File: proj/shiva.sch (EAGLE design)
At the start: 22 parts, among them J1 DM3D-SFDM, J2 ADAFRUIT_OLED_13, SW1 TACTSWB3SL-10XXP, SW2 TACTSWB3SL-10XXP, SW3 TACTSWB3SL-10XXP, SW4 TACTSWB3SL-10XXP, SW5 TACTSWB3SL-10XXP, SW6 TACTSWB3SL-10XXP, SW7 TACTSWB3SL-10XXP, U1 MCP23008QFN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

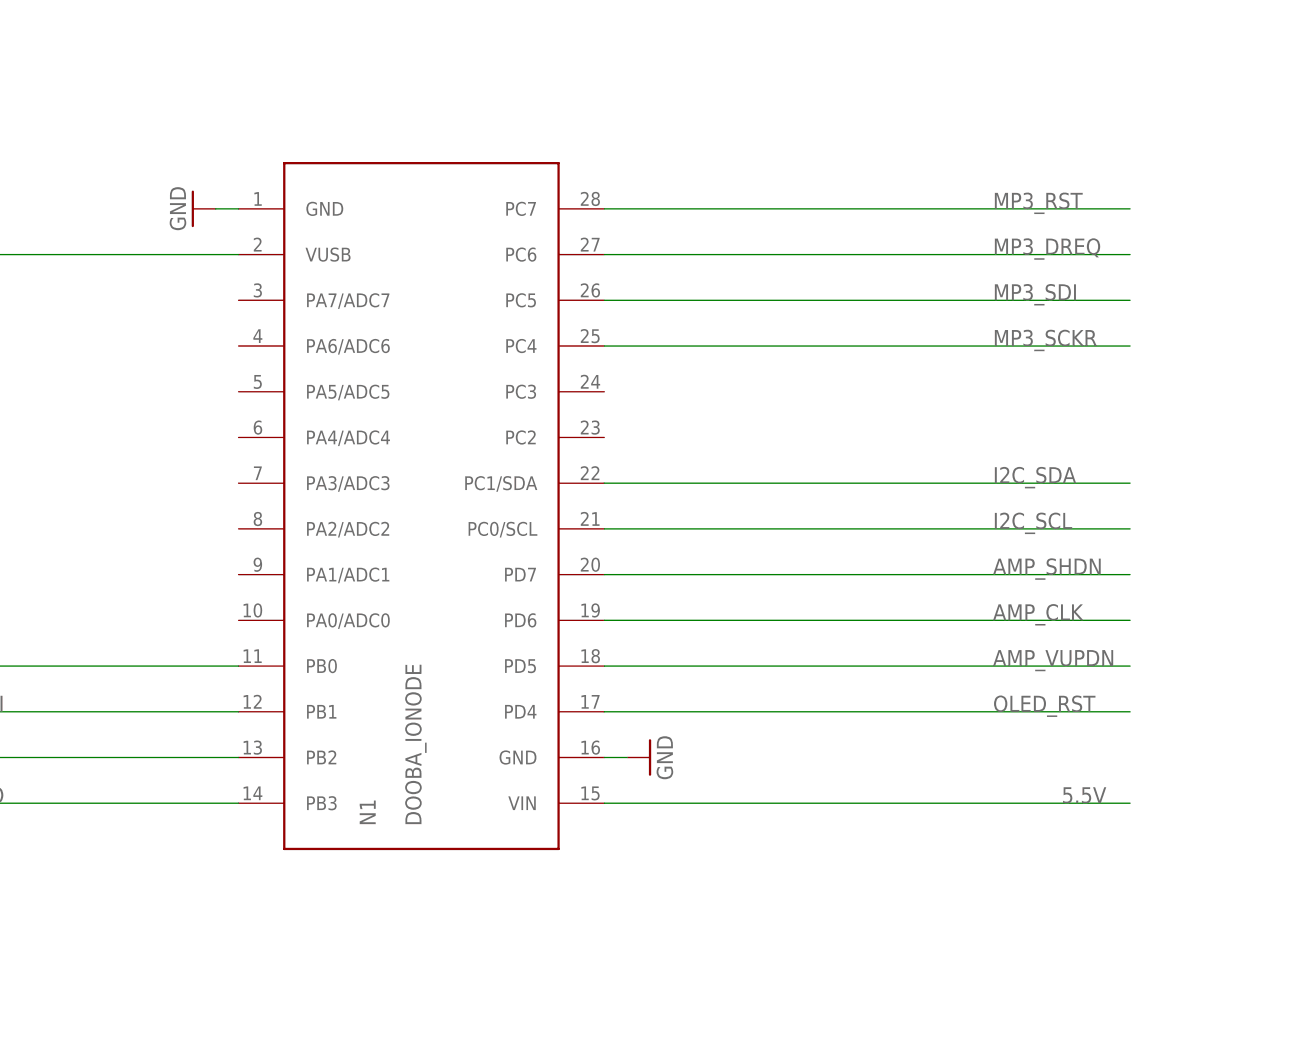
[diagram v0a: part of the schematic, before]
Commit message: Updated ioNode part in Eagle Library Integrated changes to ioNode part in Shiva board
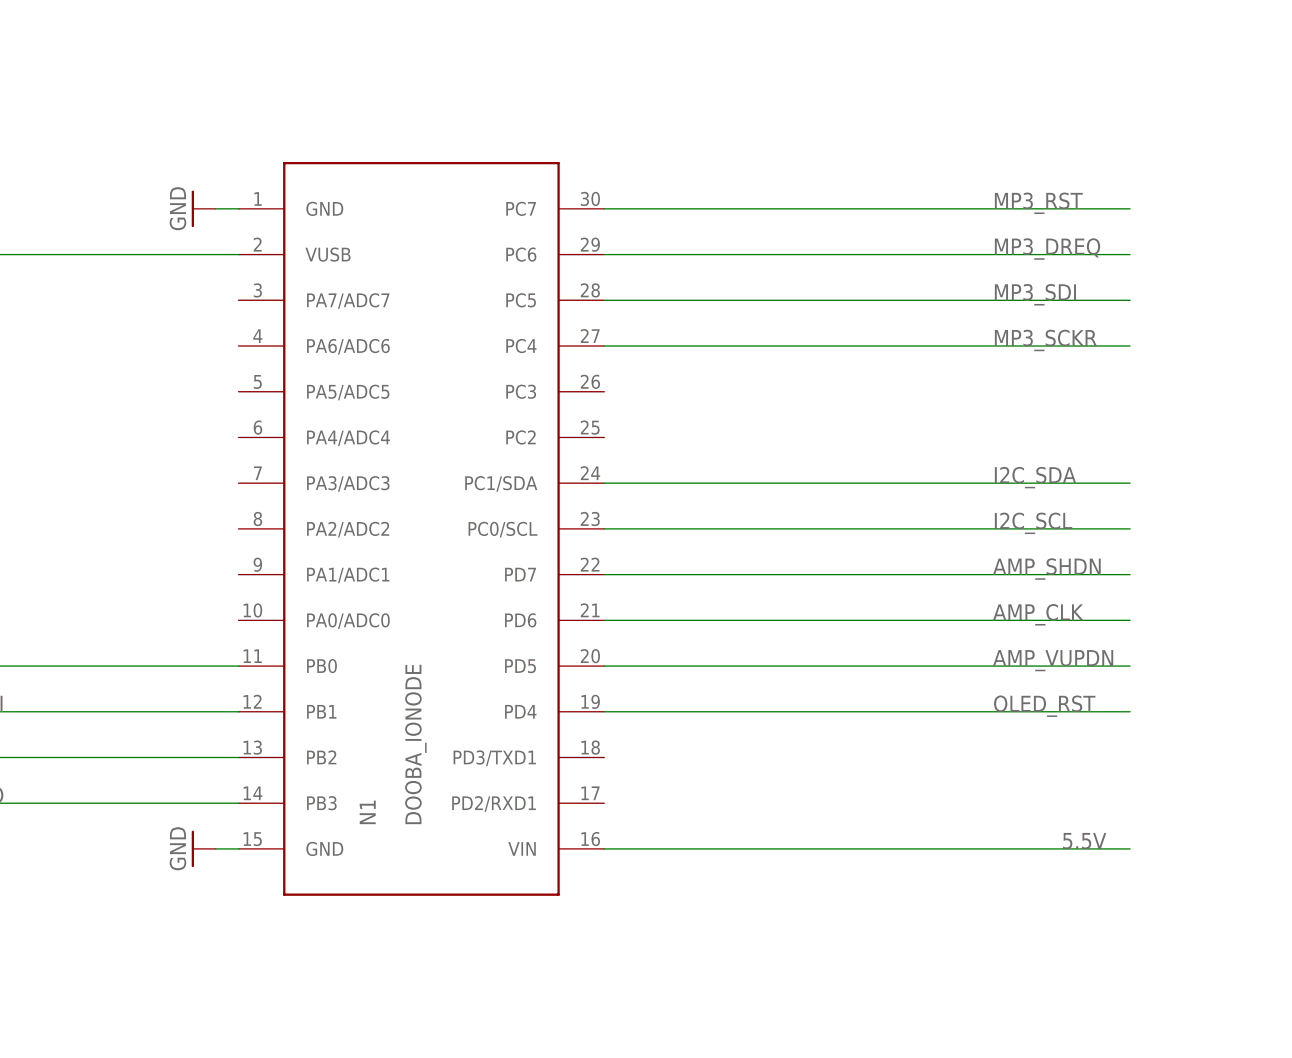
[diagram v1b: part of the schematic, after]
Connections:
- net 5.5V: now also N1.VIN@16; no longer N1.VIN@15
- net GND: now also N1.GND@15; no longer N1.GND@16
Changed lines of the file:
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@@
 <layer number="115" name="ReferenceISLANDS" color="7" fill="1" visible="yes" active="yes"/>
 <layer number="116" name="Patch_BOT" color="9" fill="4" visible="yes" active="yes"/>
+<layer number="117" name="Refs" color="11" fill="1" visible="yes" active="yes"/>
 <layer number="118" name="Rect_Pads" color="7" fill="1" visible="yes" active="yes"/>
 <layer number="121" name="_tsilk" color="7" fill="1" visible="yes" active="yes"/>
@@
 <part name="GND7" library="supply1" deviceset="GND" device=""/>
 <part name="GND8" library="supply1" deviceset="GND" device=""/>
-<part name="N1" library="dooba" deviceset="DOOBA_IONODE" device=""/>
 <part name="U2" library="dooba" deviceset="DOOBA_AECHO_NOAOUT" device=""/>
 <part name="U3" library="dooba" deviceset="DOOBA_NOMAD" device=""/>
@@
 <part name="J2" library="dooba" deviceset="ADAFRUIT_OLED_13" device=""/>
 <part name="GND31" library="supply1" deviceset="GND" device=""/>
+<part name="N1" library="dooba" deviceset="DOOBA_IONODE" device=""/>
 </parts>
 <sheets>
@@
 <instance part="GND7" gate="1" x="378.46" y="233.68" rot="R270"/>
 <instance part="GND8" gate="1" x="378.46" y="256.54" rot="R270"/>
-<instance part="N1" gate="N1" x="55.88" y="231.14"/>
 <instance part="U2" gate="U1" x="205.74" y="360.68"/>
 <instance part="U3" gate="U1" x="55.88" y="365.76"/>
@@
 <instance part="S1" gate="S1" x="53.34" y="335.28"/>
 <instance part="GND13" gate="1" x="30.48" y="264.16" rot="R270"/>
-<instance part="GND14" gate="1" x="81.28" y="203.2" rot="R90"/>
+<instance part="GND14" gate="1" x="30.48" y="193.04" rot="R270"/>
 <instance part="GND15" gate="1" x="175.26" y="373.38" rot="R270"/>
 <instance part="GND16" gate="1" x="175.26" y="363.22" rot="R270"/>
@@
 <instance part="J2" gate="J1" x="198.12" y="132.08"/>
 <instance part="GND31" gate="1" x="185.42" y="149.86" rot="R270"/>
+<instance part="N1" gate="N1" x="55.88" y="231.14"/>
 </instances>
 <busses>
@@
 </segment>
 <segment>
-<pinref part="N1" gate="N1" pin="GND@1"/>
 <pinref part="GND13" gate="1" pin="GND"/>
 <wire x1="33.02" y1="264.16" x2="35.56" y2="264.16" width="0.1524" layer="91"/>
-</segment>
-<segment>
-<pinref part="N1" gate="N1" pin="GND@16"/>
+<pinref part="N1" gate="N1" pin="GND@1"/>
+</segment>
+<segment>
 <pinref part="GND14" gate="1" pin="GND"/>
-<wire x1="78.74" y1="203.2" x2="76.2" y2="203.2" width="0.1524" layer="91"/>
+<wire x1="33.02" y1="193.04" x2="35.56" y2="193.04" width="0.1524" layer="91"/>
+<pinref part="N1" gate="N1" pin="GND@15"/>
 </segment>
 <segment>
@@
 </segment>
 <segment>
-<pinref part="N1" gate="N1" pin="VIN@15"/>
-<wire x1="76.2" y1="198.12" x2="134.62" y2="198.12" width="0.1524" layer="91"/>
-<label x="127" y="198.12" size="1.778" layer="95"/>
+<wire x1="76.2" y1="193.04" x2="134.62" y2="193.04" width="0.1524" layer="91"/>
+<label x="127" y="193.04" size="1.778" layer="95"/>
+<pinref part="N1" gate="N1" pin="VIN@16"/>
 </segment>
 <segment>
@@
 </segment>
 <segment>
-<pinref part="N1" gate="N1" pin="VUSB@2"/>
 <wire x1="35.56" y1="259.08" x2="-10.16" y2="259.08" width="0.1524" layer="91"/>
 <label x="-7.62" y="259.08" size="1.778" layer="95"/>
+<pinref part="N1" gate="N1" pin="VUSB@2"/>
 </segment>
 </net>
@@
 <net name="MP3_RST" class="0">
 <segment>
-<pinref part="N1" gate="N1" pin="PC7"/>
 <wire x1="76.2" y1="264.16" x2="134.62" y2="264.16" width="0.1524" layer="91"/>
 <label x="119.38" y="264.16" size="1.778" layer="95"/>
+<pinref part="N1" gate="N1" pin="PC7"/>
 </segment>
 <segment>
@@
 <net name="MP3_DREQ" class="0">
 <segment>
-<pinref part="N1" gate="N1" pin="PC6"/>
 <wire x1="76.2" y1="259.08" x2="134.62" y2="259.08" width="0.1524" layer="91"/>
 <label x="119.38" y="259.08" size="1.778" layer="95"/>
+<pinref part="N1" gate="N1" pin="PC6"/>
 </segment>
 <segment>
@@
 <net name="MP3_SDI" class="0">
 <segment>
-<pinref part="N1" gate="N1" pin="PC5"/>
 <wire x1="76.2" y1="254" x2="134.62" y2="254" width="0.1524" layer="91"/>
 <label x="119.38" y="254" size="1.778" layer="95"/>
+<pinref part="N1" gate="N1" pin="PC5"/>
 </segment>
 <segment>
@@
 <net name="MP3_SCKR" class="0">
 <segment>
-<pinref part="N1" gate="N1" pin="PC4"/>
 <wire x1="76.2" y1="248.92" x2="134.62" y2="248.92" width="0.1524" layer="91"/>
 <label x="119.38" y="248.92" size="1.778" layer="95"/>
+<pinref part="N1" gate="N1" pin="PC4"/>
 </segment>
 <segment>
@@
 </segment>
 <segment>
-<pinref part="N1" gate="N1" pin="PD7"/>
 <wire x1="76.2" y1="223.52" x2="134.62" y2="223.52" width="0.1524" layer="91"/>
 <label x="119.38" y="223.52" size="1.778" layer="95"/>
+<pinref part="N1" gate="N1" pin="PD7"/>
 </segment>
 </net>
@@
 </segment>
 <segment>
-<pinref part="N1" gate="N1" pin="PD6"/>
 <wire x1="76.2" y1="218.44" x2="134.62" y2="218.44" width="0.1524" layer="91"/>
 <label x="119.38" y="218.44" size="1.778" layer="95"/>
+<pinref part="N1" gate="N1" pin="PD6"/>
 </segment>
 </net>
@@
 </segment>
 <segment>
-<pinref part="N1" gate="N1" pin="PD5"/>
 <wire x1="76.2" y1="213.36" x2="134.62" y2="213.36" width="0.1524" layer="91"/>
 <label x="119.38" y="213.36" size="1.778" layer="95"/>
+<pinref part="N1" gate="N1" pin="PD5"/>
 </segment>
 </net>
@@
 </segment>
 <segment>
-<pinref part="N1" gate="N1" pin="PC0/SCL"/>
 <wire x1="76.2" y1="228.6" x2="134.62" y2="228.6" width="0.1524" layer="91"/>
 <label x="119.38" y="228.6" size="1.778" layer="95"/>
+<pinref part="N1" gate="N1" pin="PC0/SCL"/>
 </segment>
 <segment>
@@
 <net name="I2C_SDA" class="0">
 <segment>
-<pinref part="N1" gate="N1" pin="PC1/SDA"/>
 <wire x1="76.2" y1="233.68" x2="134.62" y2="233.68" width="0.1524" layer="91"/>
 <label x="119.38" y="233.68" size="1.778" layer="95"/>
+<pinref part="N1" gate="N1" pin="PC1/SDA"/>
 </segment>
 <segment>
@@
 </segment>
 <segment>
-<pinref part="N1" gate="N1" pin="PB3"/>
 <wire x1="35.56" y1="198.12" x2="-10.16" y2="198.12" width="0.1524" layer="91"/>
 <label x="-7.62" y="198.12" size="1.778" layer="95"/>
+<pinref part="N1" gate="N1" pin="PB3"/>
 </segment>
 </net>
@@
 </segment>
 <segment>
-<pinref part="N1" gate="N1" pin="PB2"/>
 <wire x1="35.56" y1="203.2" x2="-10.16" y2="203.2" width="0.1524" layer="91"/>
 <label x="-7.62" y="203.2" size="1.778" layer="95"/>
+<pinref part="N1" gate="N1" pin="PB2"/>
 </segment>
 </net>
@@
 </segment>
 <segment>
-<pinref part="N1" gate="N1" pin="PB1"/>
 <wire x1="35.56" y1="208.28" x2="-10.16" y2="208.28" width="0.1524" layer="91"/>
 <label x="-7.62" y="208.28" size="1.778" layer="95"/>
+<pinref part="N1" gate="N1" pin="PB1"/>
 </segment>
 </net>
@@
 </segment>
 <segment>
-<pinref part="N1" gate="N1" pin="PB0"/>
 <wire x1="35.56" y1="213.36" x2="-10.16" y2="213.36" width="0.1524" layer="91"/>
 <label x="-7.62" y="213.36" size="1.778" layer="95"/>
+<pinref part="N1" gate="N1" pin="PB0"/>
 </segment>
 </net>
@@
 </segment>
 <segment>
-<pinref part="N1" gate="N1" pin="PD4"/>
 <wire x1="76.2" y1="208.28" x2="134.62" y2="208.28" width="0.1524" layer="91"/>
 <label x="119.38" y="208.28" size="1.778" layer="95"/>
-</segment>
-</net>
+<pinref part="N1" gate="N1" pin="PD4"/>
+</segment>
+</net>

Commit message: Started re-designing Shiva MP3 schematic & board for hardware SPI Also, made it smaller :) @open #7
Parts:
- SW1, SW2, SW3, SW4, SW5, SW6, SW7: value TACTSWB3SL-10XXP -> TACTSW_2CK_KXT3; device dooba:TACTSWB3SL-10XXP -> dooba:TACTSW_2CK_KXT3
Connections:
- removed net MICROSD_MISO: J1.DAT0/DO, N1.PB3
- removed net MICROSD_MOSI: J1.CMD/DI, N1.PB1
- removed net MICROSD_SCK: J1.CLK/SCK, N1.PB2
- removed net MP3_SCKR: N1.PC4, U2.MP3_SCKR
- removed net MP3_SDI: N1.PC5, U2.MP3_SDI
- new net MP3_BIT_EN: U2.MP3_BIT_EN
- new net SPI_MISO: J1.DAT0/DO, N1.MISO
- new net SPI_MOSI: J1.CMD/DI, N1.MOSI, U2.MP3_SDI
- new net SPI_SCK: J1.CLK/SCK, N1.SCK, U2.MP3_SCKR
- net GND: now also N1.GND, SW1.2, SW2.2, SW3.2, SW4.2, SW5.2, SW6.2, SW7.2; no longer SW1.3, SW2.3, SW3.3, SW4.3, SW5.3, SW6.3, SW7.3

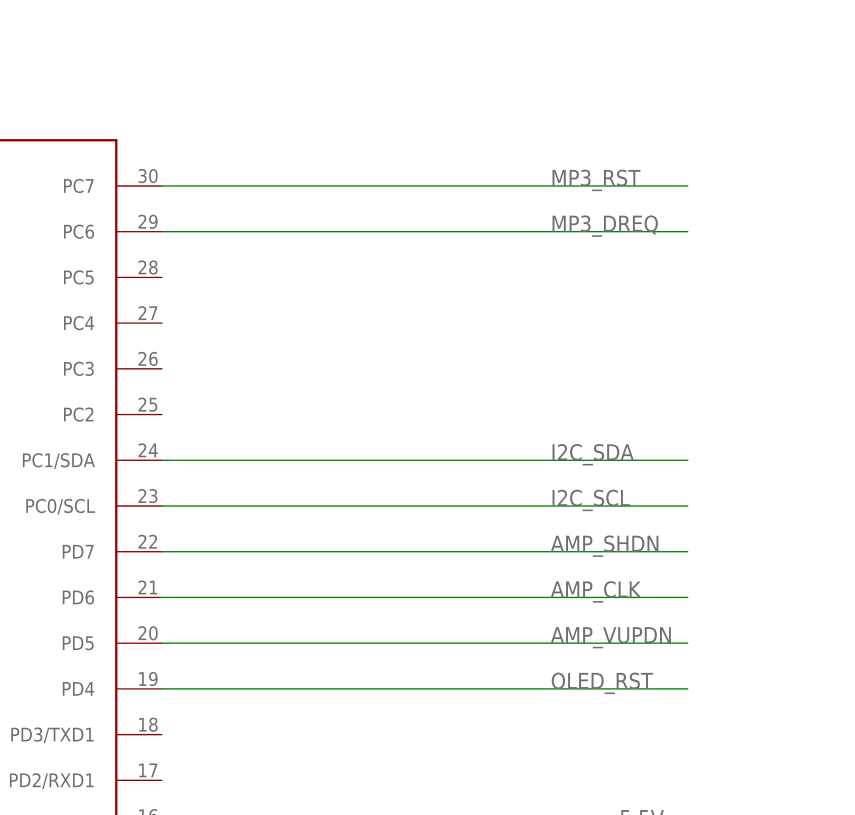
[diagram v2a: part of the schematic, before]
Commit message: Completed new Shiva board using SPI for MicroSD and Aecho Improved some QFN parts in the Eagle Library Added ref layer to Nomad for ZFPCBA @close #7
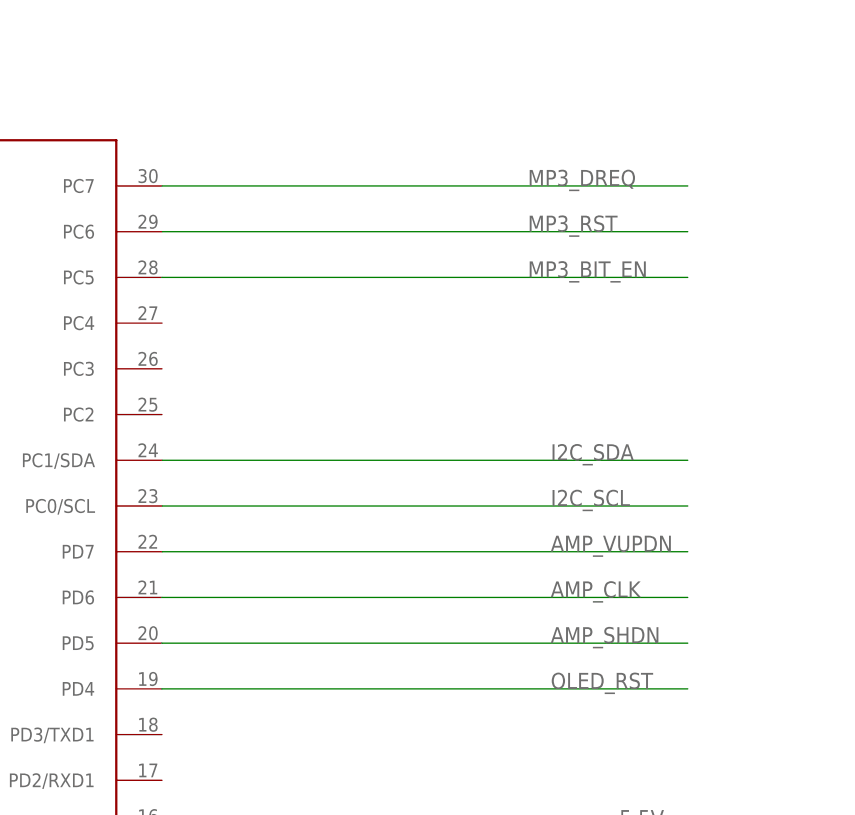
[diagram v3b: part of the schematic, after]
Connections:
- net AMP_SHDN: now also N1.PD5; no longer N1.PD7
- net AMP_VUPDN: now also N1.PD7; no longer N1.PD5
- net MP3_BIT_EN: now also N1.PC5
- net MP3_DREQ: now also N1.PC7; no longer N1.PC6
- net MP3_RST: now also N1.PC6; no longer N1.PC7
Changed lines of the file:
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@@
 <net name="MP3_RST" class="0">
-<segment>
-<wire x1="76.2" y1="309.88" x2="134.62" y2="309.88" width="0.1524" layer="91"/>
-<label x="119.38" y="309.88" size="1.778" layer="95"/>
-<pinref part="N1" gate="N1" pin="PC7"/>
-</segment>
 <segment>
 <pinref part="U2" gate="U1" pin="MP3_RST"/>
@@
 <label x="281.94" y="347.98" size="1.778" layer="95"/>
 </segment>
+<segment>
+<wire x1="76.2" y1="304.8" x2="134.62" y2="304.8" width="0.1524" layer="91"/>
+<label x="116.84" y="304.8" size="1.778" layer="95"/>
+<pinref part="N1" gate="N1" pin="PC6"/>
+</segment>
 </net>
 <net name="MP3_DREQ" class="0">
-<segment>
-<wire x1="76.2" y1="304.8" x2="134.62" y2="304.8" width="0.1524" layer="91"/>
-<label x="119.38" y="304.8" size="1.778" layer="95"/>
-<pinref part="N1" gate="N1" pin="PC6"/>
-</segment>
 <segment>
 <pinref part="U2" gate="U1" pin="MP3_DREQ"/>
@@
 <label x="281.94" y="353.06" size="1.778" layer="95"/>
 </segment>
+<segment>
+<wire x1="76.2" y1="309.88" x2="134.62" y2="309.88" width="0.1524" layer="91"/>
+<label x="116.84" y="309.88" size="1.778" layer="95"/>
+<pinref part="N1" gate="N1" pin="PC7"/>
+</segment>
 </net>
 <net name="AMP_SHDN" class="0">
@@
 </segment>
 <segment>
+<wire x1="76.2" y1="259.08" x2="134.62" y2="259.08" width="0.1524" layer="91"/>
+<label x="119.38" y="259.08" size="1.778" layer="95"/>
+<pinref part="N1" gate="N1" pin="PD5"/>
+</segment>
+</net>
+<net name="AMP_CLK" class="0">
+<segment>
+<pinref part="U2" gate="U1" pin="AMP_CLK"/>
+<wire x1="180.34" y1="353.06" x2="132.08" y2="353.06" width="0.1524" layer="91"/>
+<label x="134.62" y="353.06" size="1.778" layer="95"/>
+</segment>
+<segment>
+<wire x1="76.2" y1="264.16" x2="134.62" y2="264.16" width="0.1524" layer="91"/>
+<label x="119.38" y="264.16" size="1.778" layer="95"/>
+<pinref part="N1" gate="N1" pin="PD6"/>
+</segment>
+</net>
+<net name="AMP_VUPDN" class="0">
+<segment>
+<pinref part="U2" gate="U1" pin="AMP_VUPDN"/>
+<wire x1="180.34" y1="347.98" x2="132.08" y2="347.98" width="0.1524" layer="91"/>
+<label x="134.62" y="347.98" size="1.778" layer="95"/>
+</segment>
+<segment>
 <wire x1="76.2" y1="269.24" x2="134.62" y2="269.24" width="0.1524" layer="91"/>
 <label x="119.38" y="269.24" size="1.778" layer="95"/>
 <pinref part="N1" gate="N1" pin="PD7"/>
-</segment>
-</net>
-<net name="AMP_CLK" class="0">
-<segment>
-<pinref part="U2" gate="U1" pin="AMP_CLK"/>
-<wire x1="180.34" y1="353.06" x2="132.08" y2="353.06" width="0.1524" layer="91"/>
-<label x="134.62" y="353.06" size="1.778" layer="95"/>
-</segment>
-<segment>
-<wire x1="76.2" y1="264.16" x2="134.62" y2="264.16" width="0.1524" layer="91"/>
-<label x="119.38" y="264.16" size="1.778" layer="95"/>
-<pinref part="N1" gate="N1" pin="PD6"/>
-</segment>
-</net>
-<net name="AMP_VUPDN" class="0">
-<segment>
-<pinref part="U2" gate="U1" pin="AMP_VUPDN"/>
-<wire x1="180.34" y1="347.98" x2="132.08" y2="347.98" width="0.1524" layer="91"/>
-<label x="134.62" y="347.98" size="1.778" layer="95"/>
-</segment>
-<segment>
-<wire x1="76.2" y1="259.08" x2="134.62" y2="259.08" width="0.1524" layer="91"/>
-<label x="119.38" y="259.08" size="1.778" layer="95"/>
-<pinref part="N1" gate="N1" pin="PD5"/>
 </segment>
 </net>
@@
 <label x="281.94" y="342.9" size="1.778" layer="95"/>
 </segment>
-</net>
+<segment>
+<pinref part="N1" gate="N1" pin="PC5"/>
+<wire x1="76.2" y1="299.72" x2="134.62" y2="299.72" width="0.1524" layer="91"/>
+<label x="116.84" y="299.72" size="1.778" layer="95"/>
+</segment>
+</net>

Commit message: Updated Shiva board to use smaller oled (128x32) and joystick instead of directional buttons Added Fiddle UI Board
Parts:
- removed J2: ADAFRUIT_OLED_13, dooba:ADAFRUIT_OLED_13
- removed SW1, SW2, SW3, SW4, SW5: TACTSW_2CK_KXT3, dooba:TACTSW_2CK_KXT3
- added B1: TACTSW_5WAYSMD-7X7, dooba:TACTSW_5WAYSMD-7X7
- added OLED1: I2C-OLED-0.91, dooba:I2C-OLED-0.91
- SW6, SW7: value TACTSW_2CK_KXT3 -> TACTSW_2MICRO3X6; device dooba:TACTSW_2CK_KXT3 -> dooba:TACTSW_2MICRO3X6
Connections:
- net 3.3V: now also OLED1.VCC
- net 5.5V: no longer J2.VIN
- net GND: now also B1.COMMON, B1.GND1, B1.GND2, OLED1.GND; no longer J2.GND, SW1.2, SW2.2, SW3.2, SW4.2, SW5.2
- net I2C_SCL: now also OLED1.SCL; no longer J2.CLK
- net I2C_SDA: now also OLED1.SDA; no longer J2.DATA
- net N$1: now also B1.A; no longer SW1.1
- net N$2: now also B1.CENTER; no longer SW2.1
- net N$3: now also B1.C; no longer SW3.1
- net N$4: now also B1.D, U1.GP4; no longer SW4.1, U1.GP3
- net N$5: now also B1.B, U1.GP3; no longer SW5.1, U1.GP4
- net OLED_RST: no longer J2.RST
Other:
- moved on the sheet: C1, C2, C3, C4, C5, J1, N1, R1, R2, S1, SW6, SW7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
